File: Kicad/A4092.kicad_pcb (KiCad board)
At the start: 4 copper layers, 175.6 x 122.1 mm, 107 parts, among them CN1 Zorro3, J1 Conn_02x25_Odd_Even, J2 Conn_01x06_Pin, J3 TO-LED, J4 TO-MB, J5 Conn_02x25_Odd_Even, J7 22112042, J8 TO-A3000-LED, J9 TO-A3000-MB, SW1 219-8MST, U1 SN74ABT16543DGGR, U10 NCR53c710 SCSI Host Controller, U11 DS21S07A, U12 DS21S07A, U13 SST39SF010/020/040, U2 SN74ABT16543DGGR, U3 SN74ABT16543DGGR, U4 SN74ABT16543DGGR, U5 74LVC07APW_118, U6 SN74ABT16245ADGGR, U7 AMS1117-3.3, U8 SN74F244DB, U9 XC95144XL-TQ144, Y1 Abracon ACO-50MHz

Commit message: Routing
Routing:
- net ABOEL: track 49.3 -> 144.8 mm, vias 3 -> 5
- net D26: track 93.1 -> 90.8 mm
- net D27: track 92.3 -> 90.6 mm
- net D25: track 93.1 -> 91.8 mm
- net Z2D: track 97.9 -> 98.8 mm
- net D2Z: track 91.2 -> 92.1 mm
- net A22: track 94.3 -> 94.8 mm

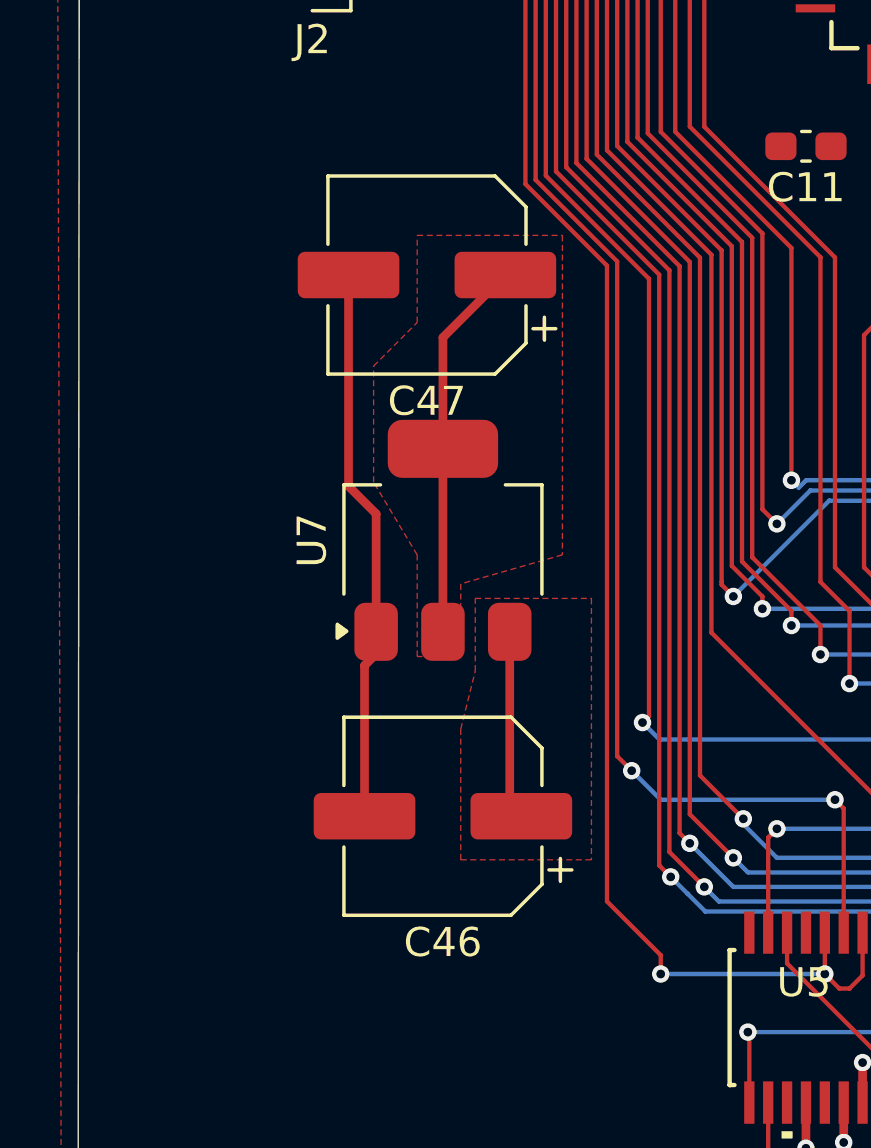
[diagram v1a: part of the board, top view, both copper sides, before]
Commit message: Replace C47 and C46 with Tantalum capacitors
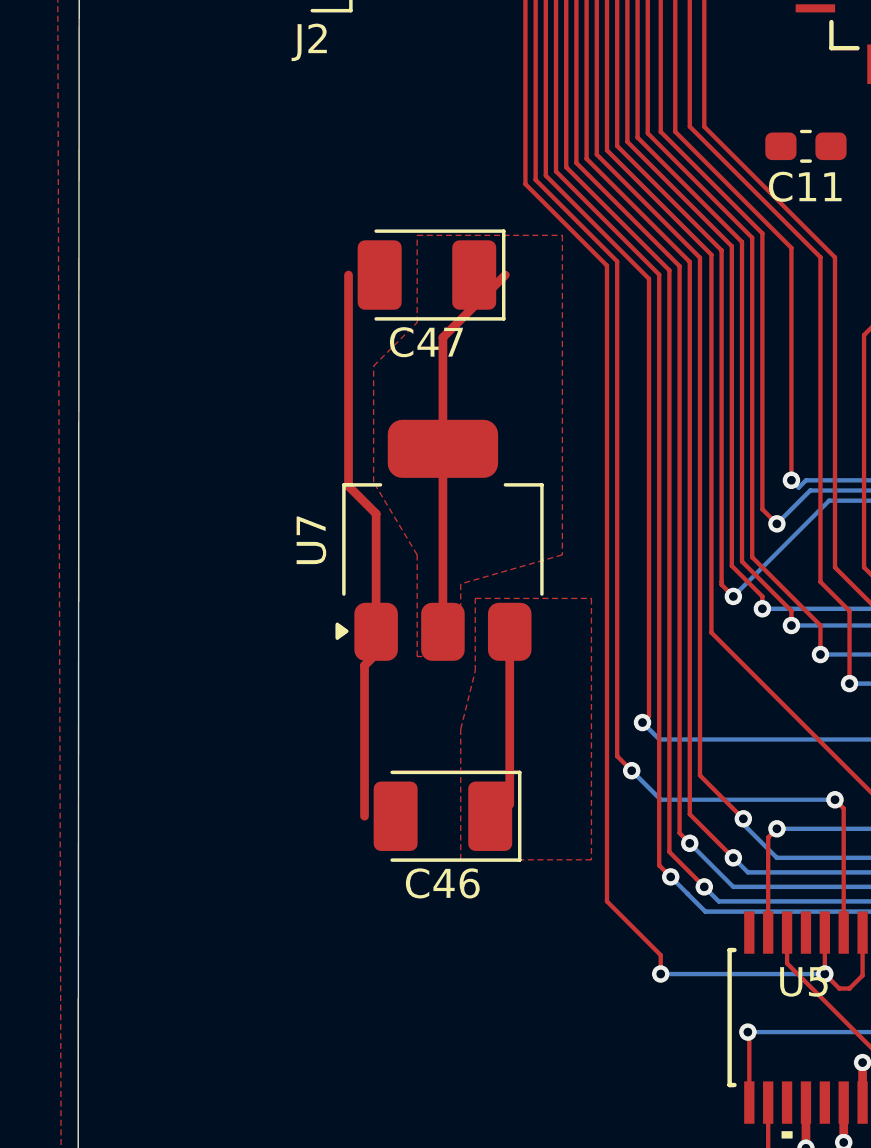
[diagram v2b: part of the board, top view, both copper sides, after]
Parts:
- C46, C47: footprint Capacitor_SMD:CP_Elec_6.3x7.7 -> Capacitor_Tantalum_SMD:CP_EIA-3528-15_AVX-H_HandSolder

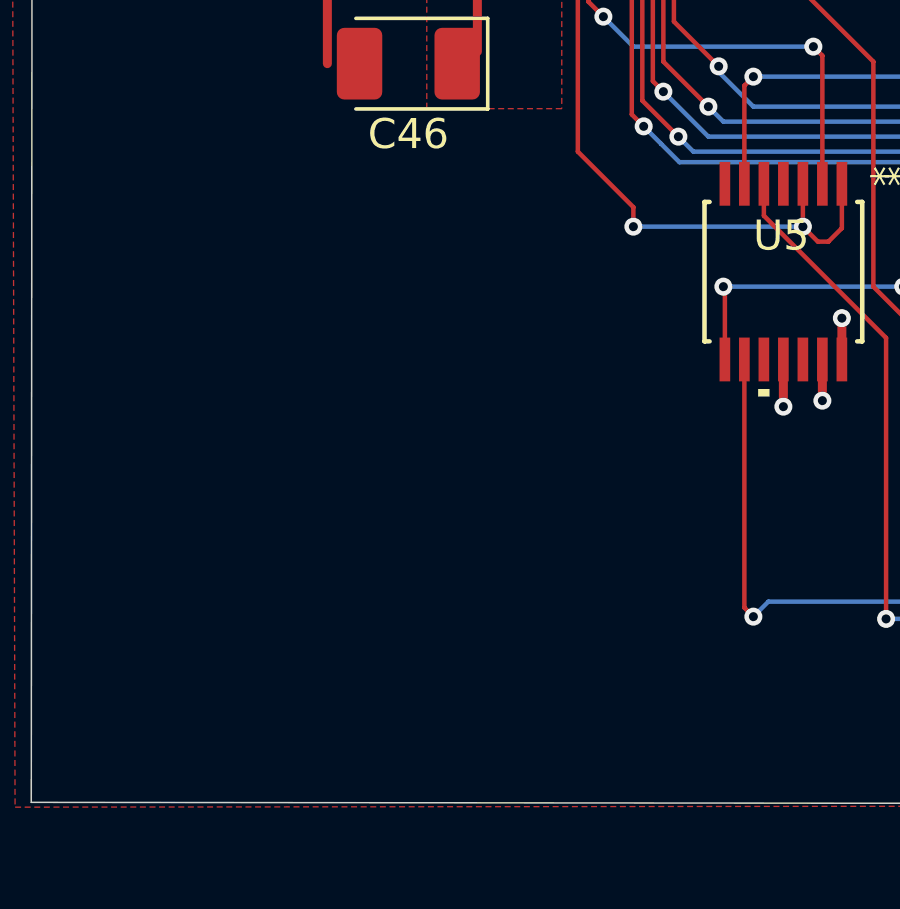
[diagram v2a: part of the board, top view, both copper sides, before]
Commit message: Add more bypass caps
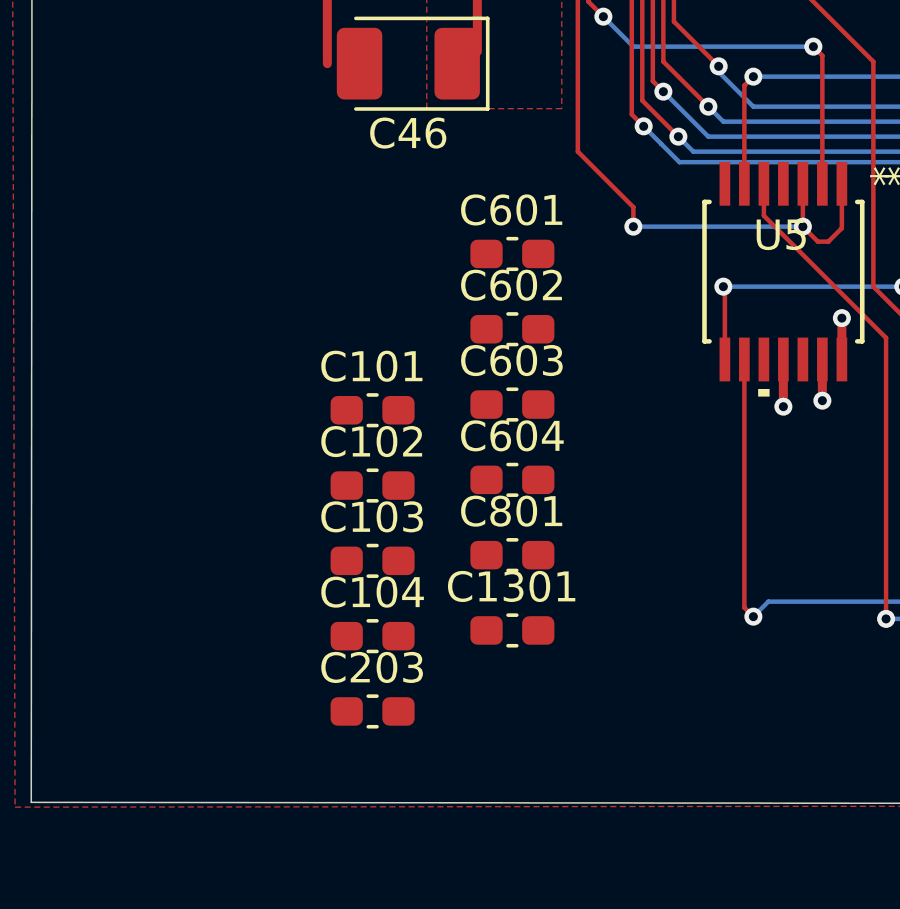
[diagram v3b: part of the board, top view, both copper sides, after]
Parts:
- added C101: 100nF, Capacitor_SMD:C_0603_1608Metric_Pad1.08x0.95mm_HandSolder, F.Cu at (60.3, 134.1)
- added C102: 100nF, Capacitor_SMD:C_0603_1608Metric_Pad1.08x0.95mm_HandSolder, F.Cu at (60.3, 136.6)
- added C103: 100nF, Capacitor_SMD:C_0603_1608Metric_Pad1.08x0.95mm_HandSolder, F.Cu at (60.3, 139.1)
- added C104: 100nF, Capacitor_SMD:C_0603_1608Metric_Pad1.08x0.95mm_HandSolder, F.Cu at (60.3, 141.7)
- added C1301: 100nF, Capacitor_SMD:C_0603_1608Metric_Pad1.08x0.95mm_HandSolder, F.Cu at (65.0, 141.5)
- added C203: 100nF, Capacitor_SMD:C_0603_1608Metric_Pad1.08x0.95mm_HandSolder, F.Cu at (60.3, 144.2)
- added C601: 100nF, Capacitor_SMD:C_0603_1608Metric_Pad1.08x0.95mm_HandSolder, F.Cu at (65.0, 128.9)
- added C602: 100nF, Capacitor_SMD:C_0603_1608Metric_Pad1.08x0.95mm_HandSolder, F.Cu at (65.0, 131.4)
- added C603: 100nF, Capacitor_SMD:C_0603_1608Metric_Pad1.08x0.95mm_HandSolder, F.Cu at (65.0, 133.9)
- added C604: 100nF, Capacitor_SMD:C_0603_1608Metric_Pad1.08x0.95mm_HandSolder, F.Cu at (65.0, 136.4)
- added C801: 100nF, Capacitor_SMD:C_0603_1608Metric_Pad1.08x0.95mm_HandSolder, F.Cu at (65.0, 138.9)
- C29: value 0.1uF -> 100nF

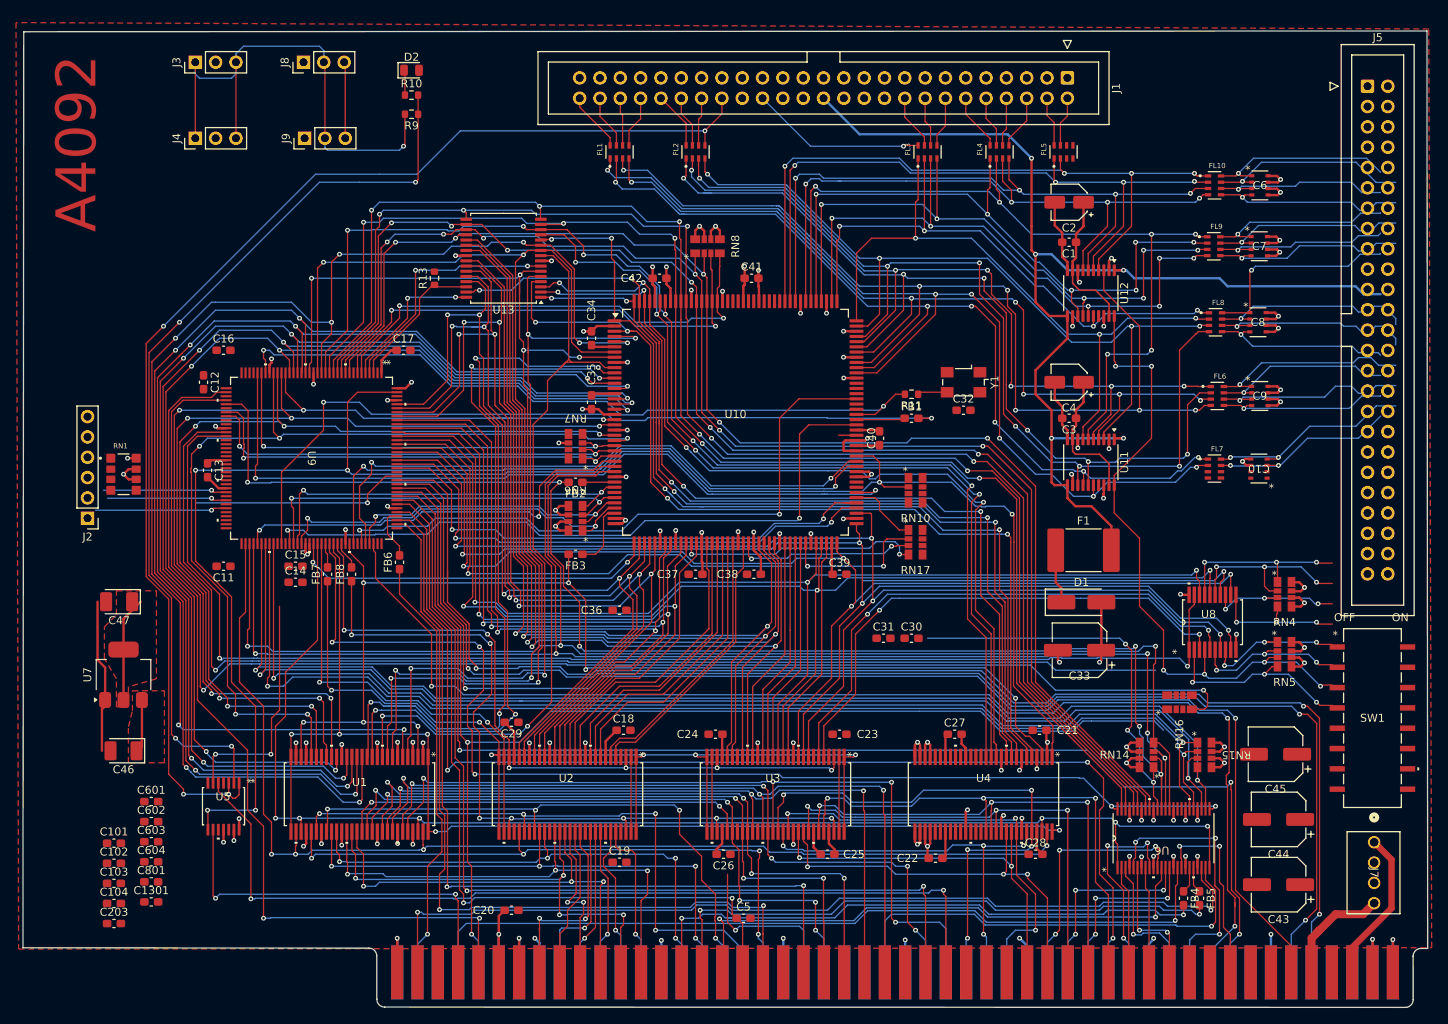
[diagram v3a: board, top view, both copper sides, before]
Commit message: Rename capacitors
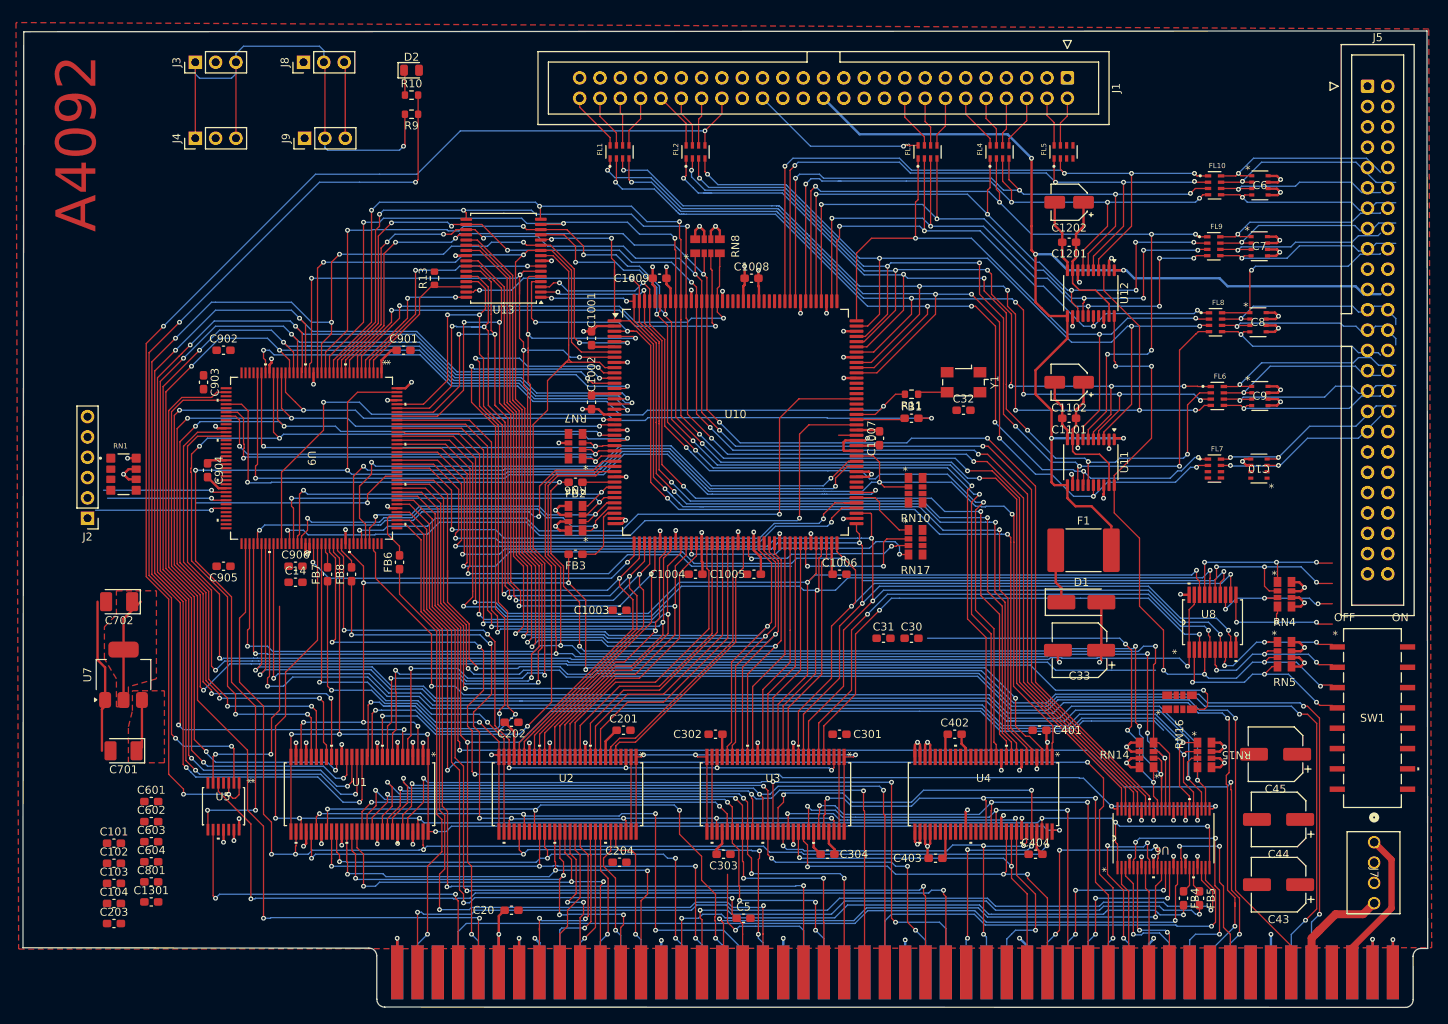
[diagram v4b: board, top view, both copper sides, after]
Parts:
- renumbered C34 to C1001, C35 to C1002, C36 to C1003, C37 to C1004, C38 to C1005, C39 to C1006, C40 to C1007, C41 to C1008, C42 to C1009, C3 to C1101, C4 to C1102, C1 to C1201, C2 to C1202, C18 to C201, C29 to C202, C19 to C204, C23 to C301, C24 to C302, C26 to C303, C25 to C304, C21 to C401, C27 to C402, C22 to C403, C28 to C404, C46 to C701, C47 to C702, C17 to C901, C16 to C902, C12 to C903, C13 to C904, C11 to C905, C15 to C906

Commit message: Fix up silkscreen across the board
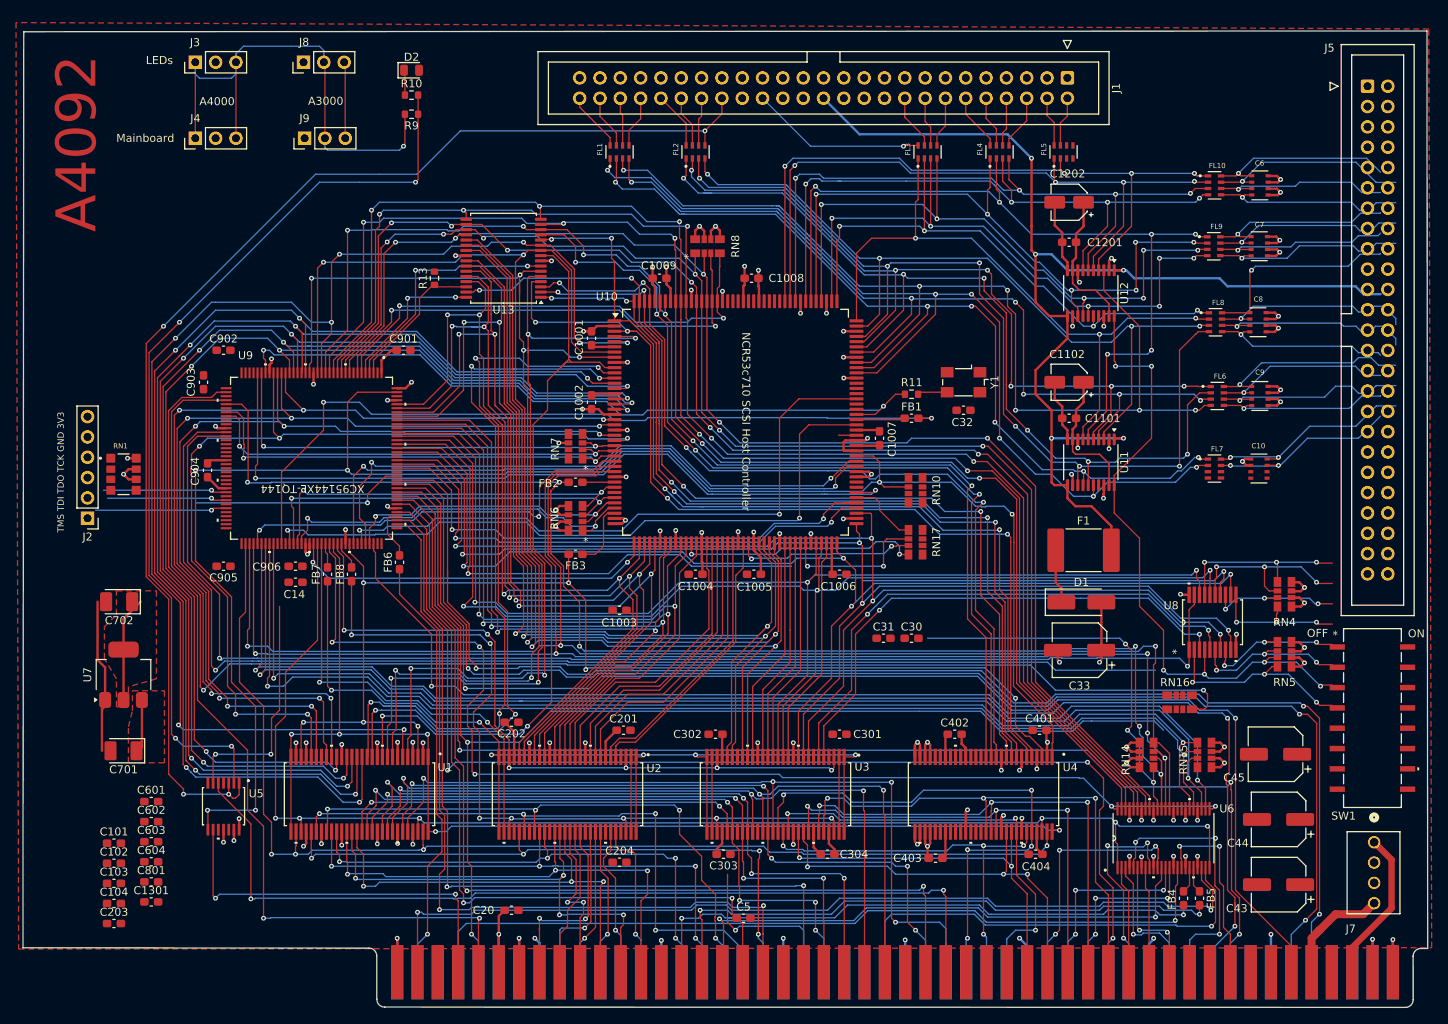
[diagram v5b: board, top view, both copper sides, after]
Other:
- board text added: "A3000"
- board text added: "A4000"
- board text added: "LEDs"
- board text added: "Mainboard"
- board text added: "NCR53c710 SCSI Host Controller"
- board text added: "TMS TDI TDO TCK GND 3V3"
- board text added: "XC95144XL-TQ144"
